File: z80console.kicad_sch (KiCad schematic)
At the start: 5 parts, among them U1 Z80CPU, U2 AT28C64B-15PU, U3 74HCT02, U4 74HC04, U5 74HCT85

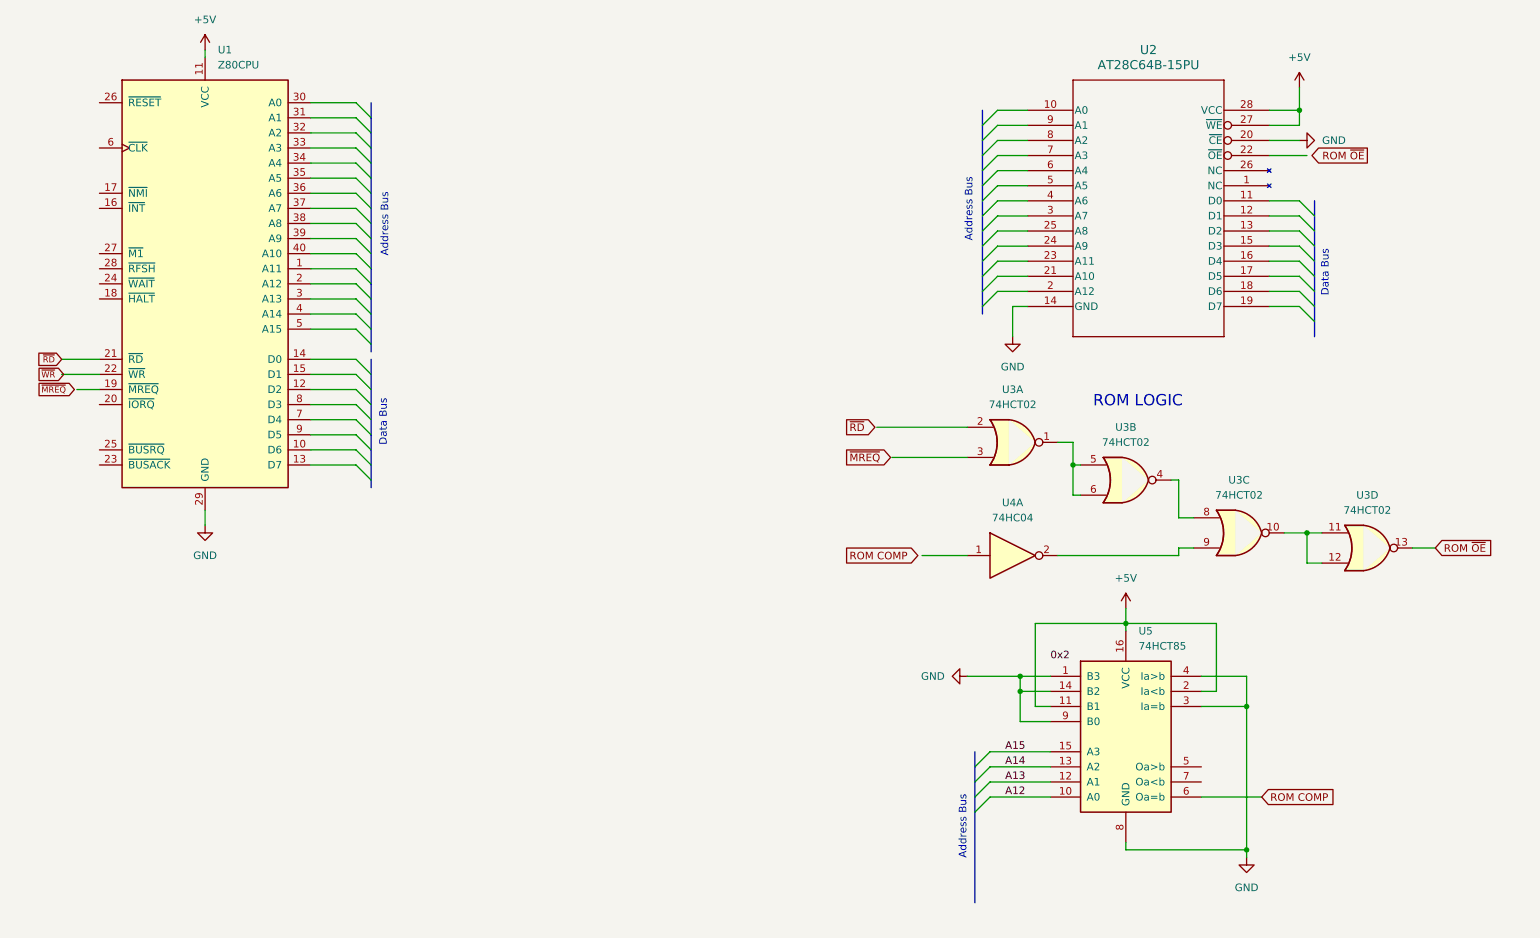
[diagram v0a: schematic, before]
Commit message: clk generation
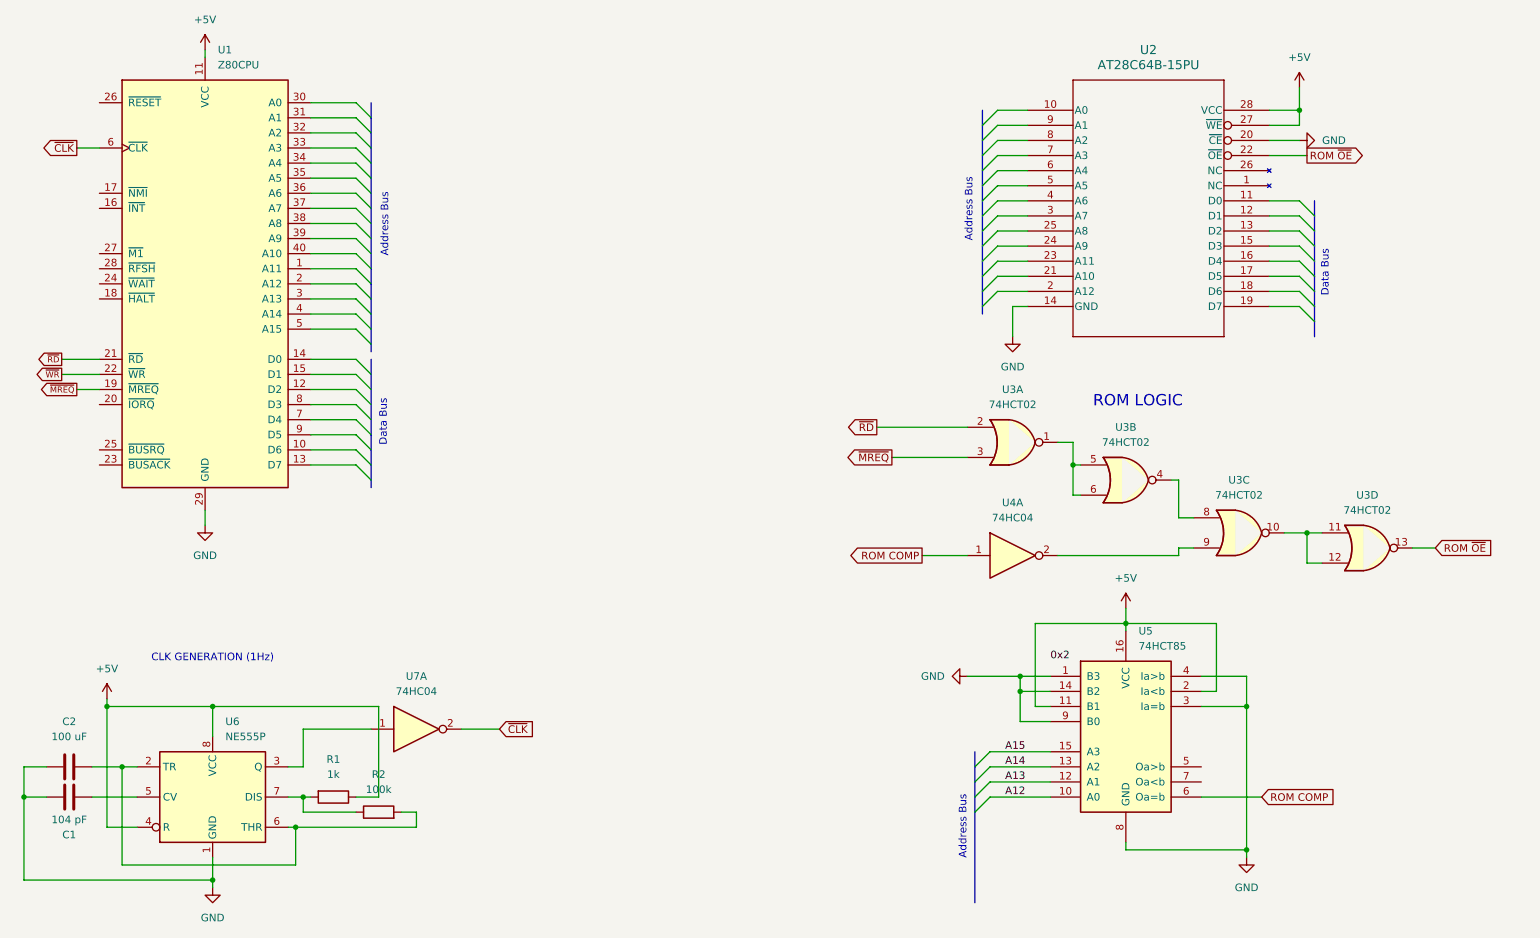
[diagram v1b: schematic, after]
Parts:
- added C1: 104 pF, symbol Device:C
- added C2: 100 uF, symbol Device:C
- added R1: 1k, symbol Device:R
- added R2: 100k, symbol Device:R
- added U6: NE555P, Package_DIP:DIP-8_W7.62mm, symbol Timer:NE555P
- added U7: 74HC04, symbol 74xx:74HC04
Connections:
- net +5V: now also R1.1, U6.4 (R), U6.8 (VCC)
- net GND: now also C1.1, C2.1, U6.1 (GND)
- net ROM COMP: now also U4.1
- net ROM ~{OE}: now also U2.22 (~{OE})
- net ~{MREQ}: now also U1.19 (~{MREQ}), U3.3
- net ~{RD}: now also U3.2
- net ~{WR}: now also U1.22 (~{WR})
- net ~{CLK}: now reaches U1.6 (~{CLK})
- net ~{CLK}: now also U7.2
- new net: R1.2, R2.1, U6.7 (DIS)
- new net: C2.2, R2.2, U6.2 (TR), U6.6 (THR)
- new net: U6.3 (Q), U7.1
- new net: C1.2, U6.5 (CV)
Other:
- note added: "CLK GENERATION (1Hz)"
